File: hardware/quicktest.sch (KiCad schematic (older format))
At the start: 43 parts

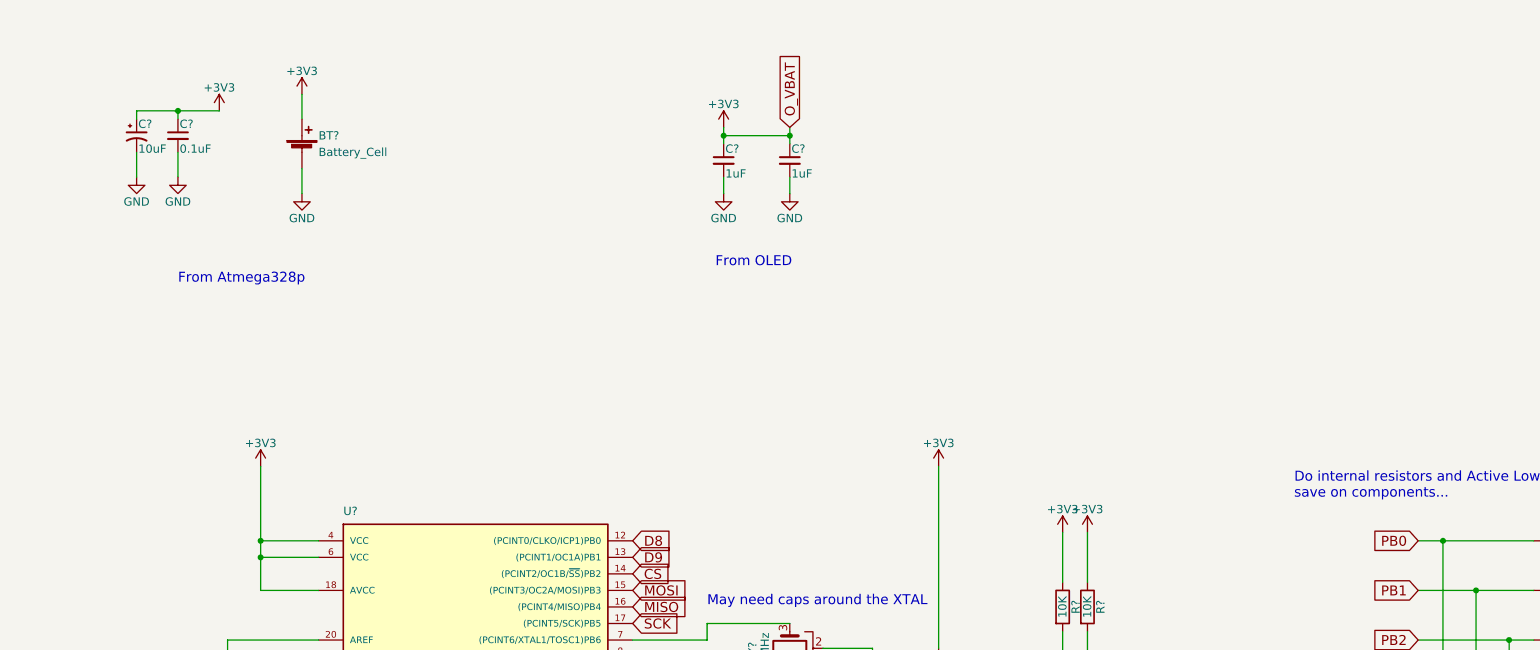
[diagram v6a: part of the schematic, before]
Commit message: filled out the vusb/vbat switching circuit more
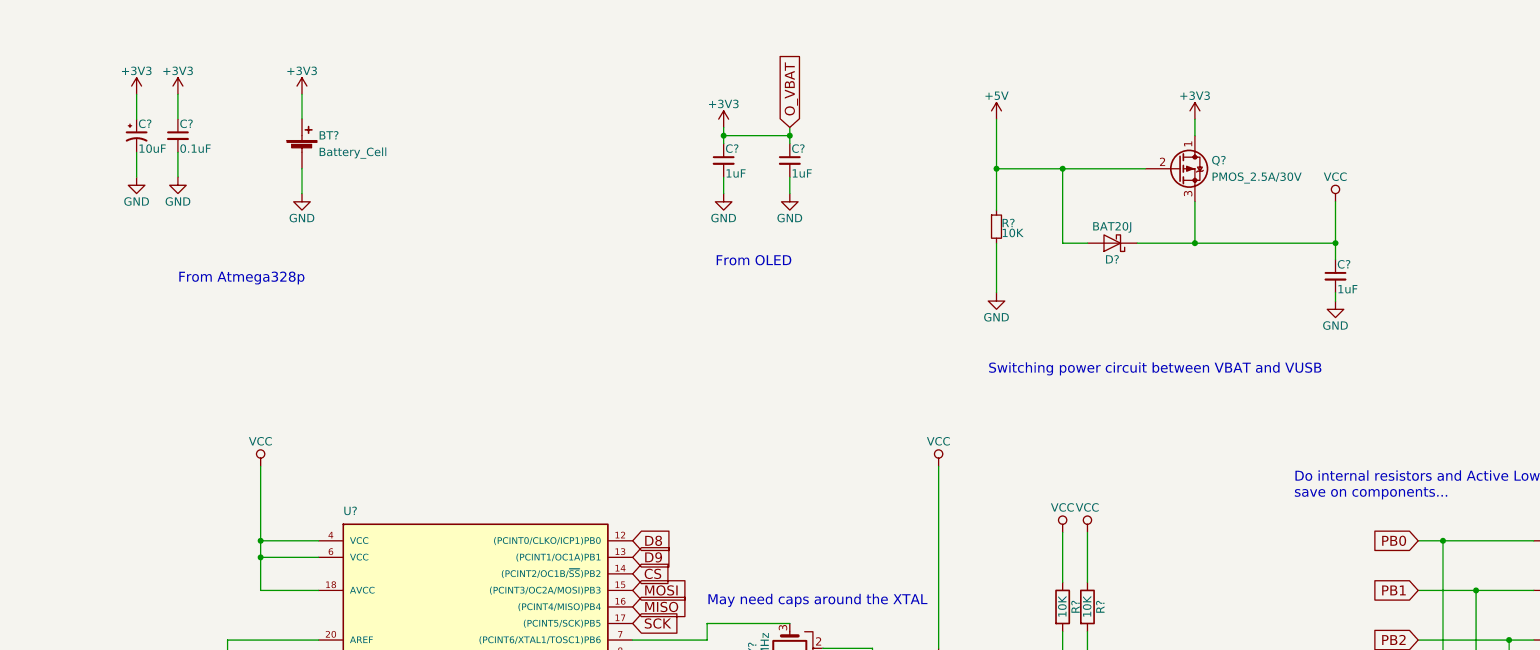
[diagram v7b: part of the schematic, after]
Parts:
- added C?: 1uF, symbol C_Small
- added D?: BAT20J, symbol D_Schottky
- added Q?: PMOS_2.5A/30V, symbol Q_PMOS_DGS
- added R?: 10K, symbol R_Small
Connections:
- net +3V3: now also Q?.1 (D); no longer R?.1, R?.1, R?.1, U?.18 (AVCC), U?.4 (VCC), U?.6 (VCC)
- net +5V: now also D?.2 (A), Q?.2 (G), R?.1
- net GND: now also C?.2, R?.2
- new net VCC: C?.1, D?.1 (K), Q?.3 (S), R?.1, R?.1, R?.1, U?.18 (AVCC), U?.4 (VCC), U?.6 (VCC)
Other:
- note added: "Switching power circuit between VBAT and VUSB"
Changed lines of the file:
@@
-$EndComp
-$Comp
-L +3V3 #PWR?
-U 1 1 596CB7C9
-P 6500 3400
-F 0 "#PWR?" H 6500 3250 50  0001 C CNN
-F 1 "+3V3" H 6500 3540 50  0000 C CNN
-F 2 "" H 6500 3400 50  0001 C CNN
-F 3 "" H 6500 3400 50  0001 C CNN
-	1    6500 3400
-	1    0    0    -1
 $EndComp
 $Comp
@@
 F 3 "" H 6650 6400 50  0001 C CNN
 	1    6650 6400
-	1    0    0    -1
-$EndComp
-$Comp
-L +3V3 #PWR?
-U 1 1 596CB863
-P 10600 3400
-F 0 "#PWR?" H 10600 3250 50  0001 C CNN
-F 1 "+3V3" H 10600 3540 50  0000 C CNN
-F 2 "" H 10600 3400 50  0001 C CNN
-F 3 "" H 10600 3400 50  0001 C CNN
-	1    10600 3400
 	1    0    0    -1
 $EndComp
@@
 	1    0    0    -1
 $EndComp
-$Comp
-L +3V3 #PWR?
-U 1 1 596E01C8
-P 11350 3800
-F 0 "#PWR?" H 11350 3650 50  0001 C CNN
-F 1 "+3V3" H 11350 3940 50  0000 C CNN
-F 2 "" H 11350 3800 50  0001 C CNN
-F 3 "" H 11350 3800 50  0001 C CNN
-	1    11350 3800
-	1    0    0    -1
-$EndComp
-$Comp
-L +3V3 #PWR?
-U 1 1 596E01E6
-P 11500 3800
-F 0 "#PWR?" H 11500 3650 50  0001 C CNN
-F 1 "+3V3" H 11500 3940 50  0000 C CNN
-F 2 "" H 11500 3800 50  0001 C CNN
-F 3 "" H 11500 3800 50  0001 C CNN
-	1    11500 3800
-	1    0    0    -1
-$EndComp
 Text GLabel 8750 5450 2    60   Input ~ 0
 RXI
@@
 L +3V3 #PWR?
 U 1 1 596E0DE2
-P 6250 1250
-F 0 "#PWR?" H 6250 1100 50  0001 C CNN
-F 1 "+3V3" H 6250 1390 50  0000 C CNN
-F 2 "" H 6250 1250 50  0001 C CNN
-F 3 "" H 6250 1250 50  0001 C CNN
-	1    6250 1250
+P 6000 1150
+F 0 "#PWR?" H 6000 1000 50  0001 C CNN
+F 1 "+3V3" H 6000 1290 50  0000 C CNN
+F 2 "" H 6000 1150 50  0001 C CNN
+F 3 "" H 6000 1150 50  0001 C CNN
+	1    6000 1150
 	1    0    0    -1
 $EndComp
@@
 Wire Wire Line
 	6000 1650 6000 1500
-Wire Wire Line
-	6250 1250 5750 1250
-Wire Wire Line
-	5750 1250 5750 1300
-Wire Wire Line
-	6000 1300 6000 1250
-Connection ~ 6000 1250
 Wire Wire Line
 	6750 1750 6750 1600
@@
 Text Notes 12750 3600 0    60   ~ 0
 Do internal resistors and Active Low?\nsave on components...
+$Comp
+L +5V #PWR?
+U 1 1 598123F7
+P 10950 1300
+F 0 "#PWR?" H 10950 1150 50  0001 C CNN
+F 1 "+5V" H 10950 1440 50  0000 C CNN
+F 2 "" H 10950 1300 50  0001 C CNN
+F 3 "" H 10950 1300 50  0001 C CNN
+	1    10950 1300
+	1    0    0    -1
+$EndComp
+$Comp
+L Q_PMOS_DGS Q?
+U 1 1 5981248C
+P 12050 1600
+F 0 "Q?" H 12250 1650 50  0000 L CNN
+F 1 "PMOS_2.5A/30V" H 12250 1550 50  0000 L CNN
+F 2 "" H 12250 1700 50  0001 C CNN
+F 3 "" H 12050 1600 50  0001 C CNN
+	1    12050 1600
+	1    0    0    -1
+$EndComp
+Wire Wire Line
+	10950 1300 10950 1850
+Wire Wire Line
+	10950 1600 11850 1600
+$Comp
+L R_Small R?
+U 1 1 598128C1
+P 10950 1950
+F 0 "R?" H 10980 1970 50  0000 L CNN
+F 1 "10K" H 10980 1910 50  0000 L CNN
+F 2 "" H 10950 1950 50  0001 C CNN
+F 3 "" H 10950 1950 50  0001 C CNN
+	1    10950 1950
+	1    0    0    -1
+$EndComp
+$Comp
+L D_Schottky D?
+U 1 1 59812A64
+P 11650 2050
+F 0 "D?" H 11650 2150 50  0000 C CNN
+F 1 "BAT20J" H 11650 1950 50  0000 C CNN
+F 2 "" H 11650 2050 50  0001 C CNN
+F 3 "" H 11650 2050 50  0001 C CNN
+	1    11650 2050
+	-1   0    0    1
+$EndComp
+$Comp
+L GND #PWR?
+U 1 1 59813057
+P 10950 2350
+F 0 "#PWR?" H 10950 2100 50  0001 C CNN
+F 1 "GND" H 10950 2200 50  0000 C CNN
+F 2 "" H 10950 2350 50  0001 C CNN
+F 3 "" H 10950 2350 50  0001 C CNN
+	1    10950 2350
+	1    0    0    -1
+$EndComp
+Wire Wire Line
+	10950 2050 10950 2350
+Connection ~ 10950 1600
+Wire Wire Line
+	11500 2050 11350 2050
+Wire Wire Line
+	11350 2050 11350 1600
+Connection ~ 11350 1600
+Wire Wire Line
+	12150 1300 12150 1400
+$Comp
+L VCC #PWR?
+U 1 1 59813673
+P 13000 1800
+F 0 "#PWR?" H 13000 1650 50  0001 C CNN
+F 1 "VCC" H 13000 1950 50  0000 C CNN
+F 2 "" H 13000 1800 50  0001 C CNN
+F 3 "" H 13000 1800 50  0001 C CNN
+	1    13000 1800
+	1    0    0    -1
+$EndComp
+$Comp
+L +3V3 #PWR?
+U 1 1 59813712
+P 12150 1300
+F 0 "#PWR?" H 12150 1150 50  0001 C CNN
+F 1 "+3V3" H 12150 1440 50  0000 C CNN
+F 2 "" H 12150 1300 50  0001 C CNN
+F 3 "" H 12150 1300 50  0001 C CNN
+	1    12150 1300
+	1    0    0    -1
+$EndComp
+Wire Wire Line
+	11800 2050 13000 2050
+Wire Wire Line
+	13000 1800 13000 2150
+Wire Wire Line
+	12150 1800 12150 2050
+Connection ~ 12150 2050
+$Comp
+L C_Small C?
+U 1 1 598061F2
+P 13000 2250
+F 0 "C?" H 13010 2320 50  0000 L CNN
+F 1 "1uF" H 13010 2170 50  0000 L CNN
+F 2 "" H 13000 2250 50  0001 C CNN
+F 3 "" H 13000 2250 50  0001 C CNN
+	1    13000 2250
+	1    0    0    -1
+$EndComp
+$Comp
+L GND #PWR?
+U 1 1 59806297
+P 13000 2400
+F 0 "#PWR?" H 13000 2150 50  0001 C CNN
+F 1 "GND" H 13000 2250 50  0000 C CNN
+F 2 "" H 13000 2400 50  0001 C CNN
+F 3 "" H 13000 2400 50  0001 C CNN
+	1    13000 2400
+	1    0    0    -1
+$EndComp
+Wire Wire Line
+	13000 2400 13000 2350
+Connection ~ 13000 2050
+Text Notes 10900 2850 0    60   ~ 0
+Switching power circuit between VBAT and VUSB
+$Comp
+L VCC #PWR?
+U 1 1 5980975B
+P 6500 3400
+F 0 "#PWR?" H 6500 3250 50  0001 C CNN
+F 1 "VCC" H 6500 3550 50  0000 C CNN
+F 2 "" H 6500 3400 50  0001 C CNN
+F 3 "" H 6500 3400 50  0001 C CNN
+	1    6500 3400
+	1    0    0    -1
+$EndComp
+$Comp
+L VCC #PWR?
+U 1 1 5980BBF9
+P 10600 3400
+F 0 "#PWR?" H 10600 3250 50  0001 C CNN
+F 1 "VCC" H 10600 3550 50  0000 C CNN
+F 2 "" H 10600 3400 50  0001 C CNN
+F 3 "" H 10600 3400 50  0001 C CNN
+	1    10600 3400
+	1    0    0    -1
+$EndComp
+$Comp
+L VCC #PWR?
+U 1 1 5980BCCB
+P 11350 3800
+F 0 "#PWR?" H 11350 3650 50  0001 C CNN
+F 1 "VCC" H 11350 3950 50  0000 C CNN
+F 2 "" H 11350 3800 50  0001 C CNN
+F 3 "" H 11350 3800 50  0001 C CNN
+	1    11350 3800
+	1    0    0    -1
+$EndComp
+$Comp
+L VCC #PWR?
+U 1 1 5980BD3D
+P 11500 3800
+F 0 "#PWR?" H 11500 3650 50  0001 C CNN
+F 1 "VCC" H 11500 3950 50  0000 C CNN
+F 2 "" H 11500 3800 50  0001 C CNN
+F 3 "" H 11500 3800 50  0001 C CNN
+	1    11500 3800
+	1    0    0    -1
+$EndComp
+$Comp
+L +3V3 #PWR?
+U 1 1 598457E5
+P 5750 1150
+F 0 "#PWR?" H 5750 1000 50  0001 C CNN
+F 1 "+3V3" H 5750 1290 50  0000 C CNN
+F 2 "" H 5750 1150 50  0001 C CNN
+F 3 "" H 5750 1150 50  0001 C CNN
+	1    5750 1150
+	1    0    0    -1
+$EndComp
+Wire Wire Line
+	5750 1150 5750 1300
+Wire Wire Line
+	6000 1150 6000 1300
 $EndSCHEMATC
